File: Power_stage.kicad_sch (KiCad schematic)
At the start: 20 parts, among them Q1 BUK7M9R9-60EX, Q10 BUK7M9R9-60EX, Q11 BUK7M9R9-60EX, Q12 BUK7M9R9-60EX, Q2 BUK7M9R9-60EX, Q3 BUK7M9R9-60EX, Q4 BUK7M9R9-60EX, Q5 BUK7M9R9-60EX, Q6 BUK7M9R9-60EX, Q7 BUK7M9R9-60EX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

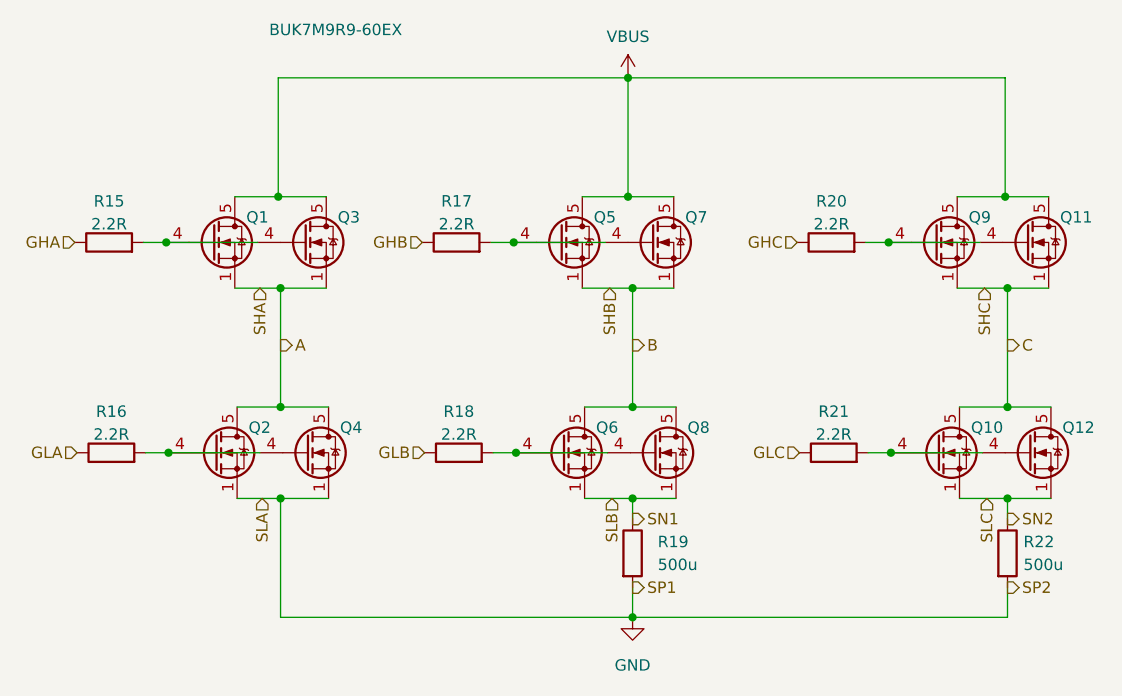
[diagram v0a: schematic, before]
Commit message: Using DRV8353 with built in current sense
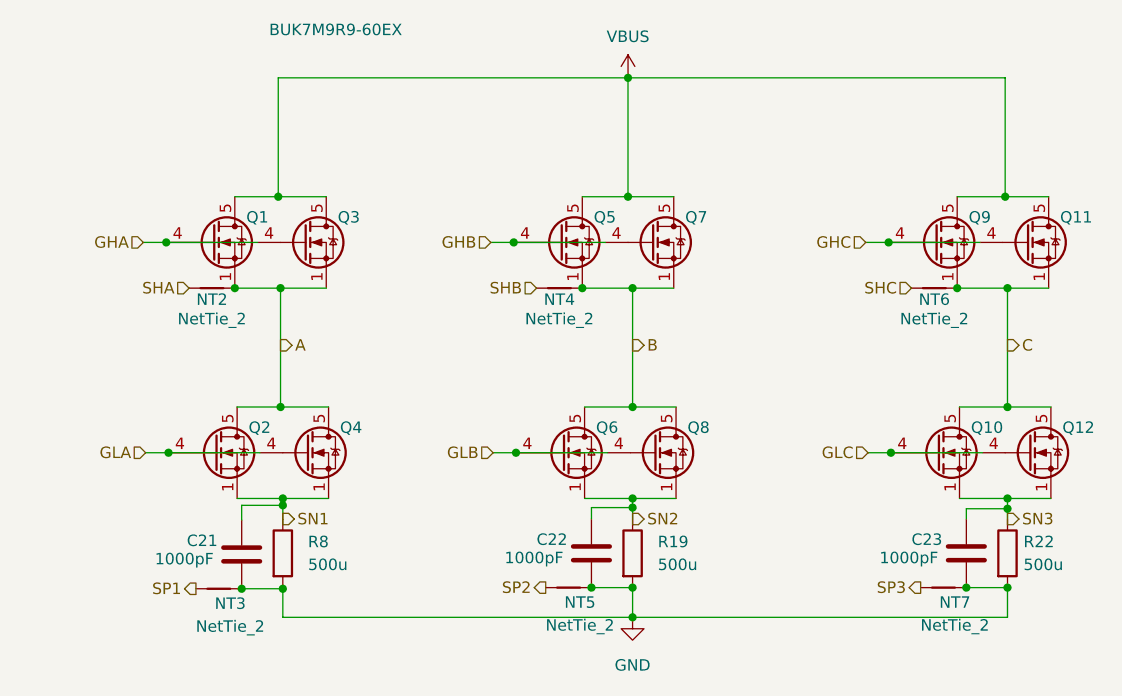
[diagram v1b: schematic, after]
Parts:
- removed R15, R16, R17, R18, R20, R21: 2.2R, Resistor_SMD:R_0402_1005Metric, symbol Device:R
- added C21, C22, C23: 1000pF, Capacitor_SMD:C_0402_1005Metric, symbol Device:C
- added NT2, NT3, NT4, NT5, NT6, NT7: NetTie_2, NetTie:NetTie-2_SMD_Pad0.5mm, symbol Device:NetTie_2
- added R8: 500u, Resistor_SMD:R_2010_5025Metric, symbol Device:R
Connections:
- net A: now also NT2.2
- net B: now also NT4.2
- net C: now also NT6.2
- net GHA: now also Q1.4 (G), Q3.4 (G)
- net GHB: now also Q5.4 (G), Q7.4 (G)
- net GHC: now also Q11.4 (G), Q9.4 (G)
- net GLA: now also Q2.4 (G), Q4.4 (G)
- net GLB: now also Q6.4 (G), Q8.4 (G)
- net GLC: now also Q10.4 (G), Q12.4 (G)
- net GND: now also C21.2, C22.2, C23.2, NT3.2, NT5.2, NT7.2, R8.2; no longer Q2.1 (S), Q2.2 (S), Q2.3 (S), Q4.1 (S), Q4.2 (S), Q4.3 (S)
- net SLB renamed SN2
- net SN2: now also C22.1
- net SLC renamed SN3
- net SN3: now also C23.1
- new net SHA: NT2.1
- new net SHB: NT4.1
- new net SHC: NT6.1
- new net SN1: C21.1, Q2.1 (S), Q2.2 (S), Q2.3 (S), Q4.1 (S), Q4.2 (S), Q4.3 (S), R8.1
- new net SP1: NT3.1
- new net SP2: NT5.1
- new net SP3: NT7.1

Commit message: Adding step
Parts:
- R19, R22, R8: value 500u -> 0.002R; footprint Resistor_SMD:R_2010_5025Metric -> Resistor_SMD:R_2816_7142Metric
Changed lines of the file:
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@@
       (effects (font (size 1.27 1.27)) (justify left))
     )
-    (property "Value" "500u" (id 1) (at 114.3 87.8839 0)
-      (effects (font (size 1.27 1.27)) (justify left))
-    )
-    (property "Footprint" "Resistor_SMD:R_2010_5025Metric" (id 2) (at 109.728 86.614 90)
+    (property "Value" "0.002R" (id 1) (at 114.3 87.8839 0)
+      (effects (font (size 1.27 1.27)) (justify left))
+    )
+    (property "Footprint" "Resistor_SMD:R_2816_7142Metric" (id 2) (at 109.728 86.614 90)
       (effects (font (size 1.27 1.27)) hide)
     )
@@
   (symbol (lib_id "Device:R") (at 72.644 86.614 0) (unit 1)
     (in_bom yes) (on_board yes) (fields_autoplaced)
-    (property "Reference" "R8" (id 0) (at 75.438 85.3439 0)
-      (effects (font (size 1.27 1.27)) (justify left))
-    )
-    (property "Value" "500u" (id 1) (at 75.438 87.8839 0)
-      (effects (font (size 1.27 1.27)) (justify left))
-    )
-    (property "Footprint" "Resistor_SMD:R_2010_5025Metric" (id 2) (at 70.866 86.614 90)
+    (property "Reference" "R8" (id 0) (at 74.93 85.3439 0)
+      (effects (font (size 1.27 1.27)) (justify left))
+    )
+    (property "Value" "0.002R" (id 1) (at 74.93 87.8839 0)
+      (effects (font (size 1.27 1.27)) (justify left))
+    )
+    (property "Footprint" "Resistor_SMD:R_2816_7142Metric" (id 2) (at 70.866 86.614 90)
       (effects (font (size 1.27 1.27)) hide)
     )
@@
       (effects (font (size 1.27 1.27)) (justify left))
     )
-    (property "Value" "500u" (id 1) (at 154.94 87.8839 0)
-      (effects (font (size 1.27 1.27)) (justify left))
-    )
-    (property "Footprint" "Resistor_SMD:R_2010_5025Metric" (id 2) (at 151.384 86.614 90)
-      (effects (font (size 1.27 1.27)) hide)
-    )
+    (property "Value" "0.002R" (id 1) (at 154.94 87.8839 0)
+      (effects (font (size 1.27 1.27)) (justify left))
+    )
+    (property "Footprint" "Resistor_SMD:R_2816_7142Metric" (id 2) (at 151.384 86.614 90)
+      (effects (font (size 1.27 1.27)) hide)
+    )

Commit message: init routing done
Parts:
- R19, R22, R8: footprint Resistor_SMD:R_2816_7142Metric -> Resistor_SMD:R_2512_6332Metric
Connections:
- net A: now also NT4.2, Q5.1 (S), Q5.2 (S), Q5.3 (S), Q6.5 (D), Q7.1 (S), Q7.2 (S), Q7.3 (S), Q8.5 (D); no longer NT2.2, Q1.1 (S), Q1.2 (S), Q1.3 (S), Q2.5 (D), Q3.1 (S), Q3.2 (S), Q3.3 (S), Q4.5 (D)
- net B: now also NT2.2, Q1.1 (S), Q1.2 (S), Q1.3 (S), Q2.5 (D), Q3.1 (S), Q3.2 (S), Q3.3 (S), Q4.5 (D); no longer NT4.2, Q5.1 (S), Q5.2 (S), Q5.3 (S), Q6.5 (D), Q7.1 (S), Q7.2 (S), Q7.3 (S), Q8.5 (D)
- net GHA: now also Q5.4 (G), Q7.4 (G); no longer Q1.4 (G), Q3.4 (G)
- net GHB: now also Q1.4 (G), Q3.4 (G); no longer Q5.4 (G), Q7.4 (G)
- net GLA: now also Q6.4 (G), Q8.4 (G); no longer Q2.4 (G), Q4.4 (G)
- net GLB: now also Q2.4 (G), Q4.4 (G); no longer Q6.4 (G), Q8.4 (G)
- net SHA: now also NT4.1; no longer NT2.1
- net SHB: now also NT2.1; no longer NT4.1
- net SN1: now also C22.1, Q6.1 (S), Q6.2 (S), Q6.3 (S), Q8.1 (S), Q8.2 (S), Q8.3 (S), R19.1; no longer C21.1, Q2.1 (S), Q2.2 (S), Q2.3 (S), Q4.1 (S), Q4.2 (S), Q4.3 (S), R8.1
- net SN2: now also C21.1, Q2.1 (S), Q2.2 (S), Q2.3 (S), Q4.1 (S), Q4.2 (S), Q4.3 (S), R8.1; no longer C22.1, Q6.1 (S), Q6.2 (S), Q6.3 (S), Q8.1 (S), Q8.2 (S), Q8.3 (S), R19.1
- net SP1: now also NT5.1; no longer NT3.1
- net SP2: now also NT3.1; no longer NT5.1
